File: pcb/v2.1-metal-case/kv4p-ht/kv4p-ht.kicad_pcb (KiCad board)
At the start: 4 copper layers, 80 x 47 mm, 71 parts, among them J1 Antenna, J5 USB-C Socket, Q1 SS8050, Q2 SS8050, Q3 AO3400A, SW3 Reset, SW4 Program, U1 DRA/SA818, U2 AZ1117H-3.3TRG1, U4 CP2102N-A02-GQFN24, U5 ESP32-WROOM-32E-N4

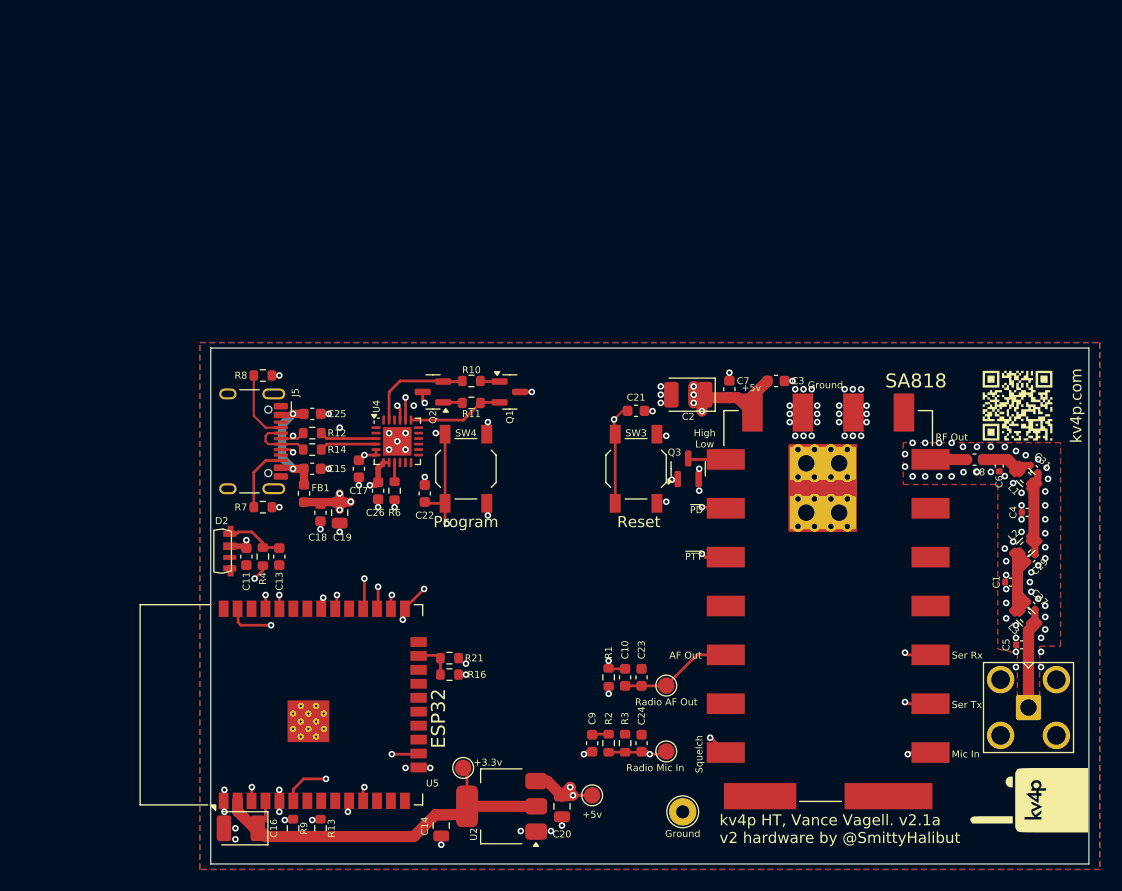
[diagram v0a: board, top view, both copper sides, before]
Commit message: Working on a different case version of kv4p board.
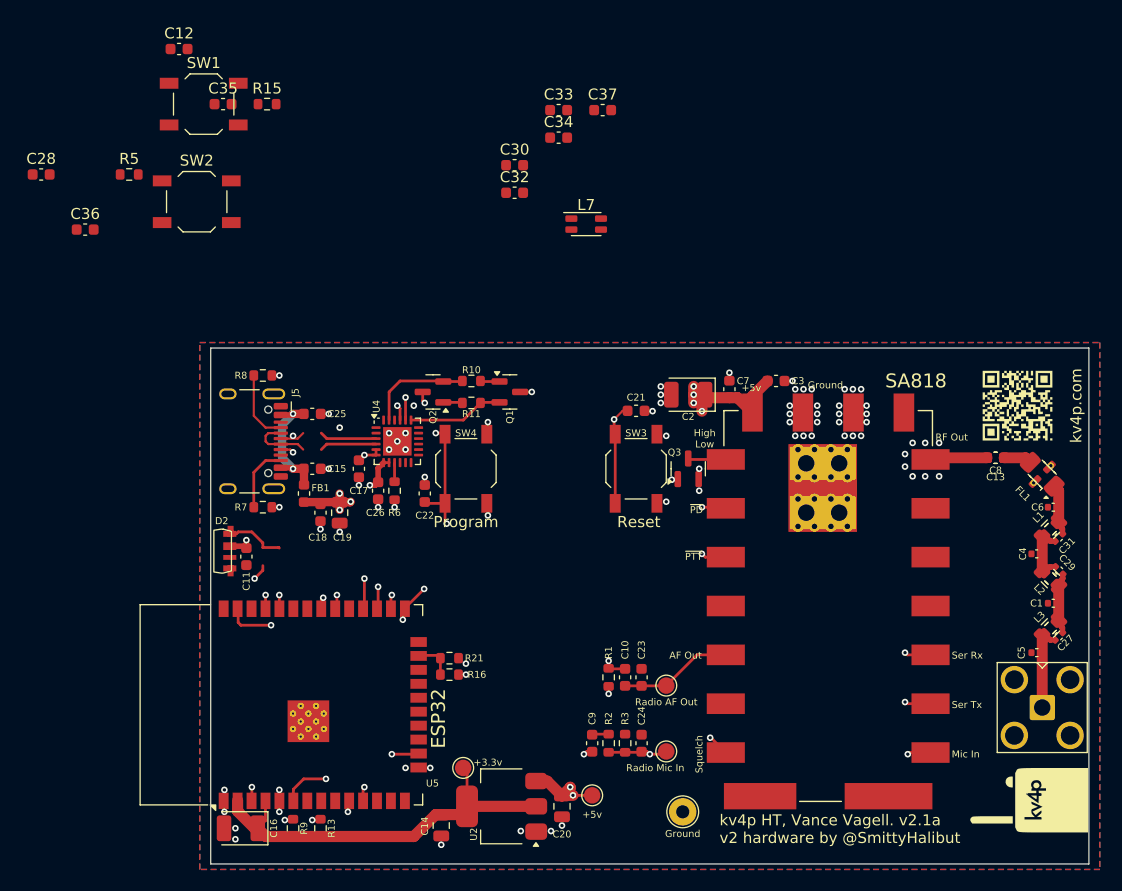
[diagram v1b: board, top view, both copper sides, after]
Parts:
- added C12: 2.2nF Tuned VHF, Capacitor_SMD:C_0603_1608Metric, F.Cu at (187.1, 43.3)
- added C28: 2.2nF Tuned VHF, Capacitor_SMD:C_0603_1608Metric, F.Cu at (174.6, 54.7)
- added C30: 220pF Tune UHF, Capacitor_SMD:C_0603_1608Metric, F.Cu at (217.7, 53.8)
- added C32: 220pF Tune UHF, Capacitor_SMD:C_0603_1608Metric, F.Cu at (217.7, 56.4)
- added C33: 220pF Tune UHF, Capacitor_SMD:C_0603_1608Metric, F.Cu at (221.7, 48.8)
- added C34: 220pF Tune UHF, Capacitor_SMD:C_0603_1608Metric, F.Cu at (221.7, 51.3)
- added C35: 220pF Tune UHF, Capacitor_SMD:C_0603_1608Metric, F.Cu at (191.1, 48.3)
- added C36: 220pF Tune UHF, Capacitor_SMD:C_0603_1608Metric, F.Cu at (178.6, 59.7)
- added C37: 220pF Tune UHF, Capacitor_SMD:C_0603_1608Metric, F.Cu at (225.7, 48.8)
- added FL1: LFCN-490+, Filter:Filter_Mini-Circuits_FV1206, F.Cu at (265.8, 82.0)
- added L7: CMCC, Inductor_SMD:L_CommonMode_Wurth_WE-CNSW-1206, F.Cu at (224.2, 59.2)
- added R15: 10k, Resistor_SMD:R_0603_1608Metric, F.Cu at (195.1, 48.3)
- added R17: 0R, Resistor_SMD:R_0603_1608Metric, F.Cu at (266.5, 87.0)
- added R5: 10k, Resistor_SMD:R_0603_1608Metric, F.Cu at (182.6, 54.7)
- added SW1: Program, Button_Switch_SMD:SW_SPST_TL3342, F.Cu at (189.4, 48.3)
- added SW2: Program, Button_Switch_SMD:SW_SPST_TL3342, F.Cu at (188.7, 57.2)
- C13: value 2.2nF Tuned VHF -> 220pF Tune UHF
- R12, R14: value 27R -> 0R
- R4: value 100R -> 0R; footprint Resistor_SMD:R_0603_1608Metric -> Resistor_SMD:R_1206_3216Metric
- moved R4 71.4 mm to (265.8, 82.0), turned to -45 degrees
- moved R12 69.6 mm to (266.5, 96.0), turned to -135 degrees
- moved R14 68.3 mm to (266.5, 91.5), turned to -45 degrees
- moved C13 65.9 mm to (261.5, 80.5), turned to 180 degrees
- moved C31 6.61 mm to (267.2, 87.8), turned to 45 degrees
- moved C6 6.18 mm to (266.8, 85.0), turned to 0 degrees
- moved L1 5.22 mm to (266.5, 87.0), turned to 45 degrees
- moved L6 5.22 mm to (266.5, 87.0), turned to 45 degrees
- moved C1 4.35 mm to (266.8, 93.8)
- moved C4 3.88 mm to (265.2, 89.2)
- moved C27 3.73 mm to (267.2, 96.8), turned to 45 degrees
- moved L2 3.64 mm to (266.5, 91.5), turned to 135 degrees
- moved L5 3.64 mm to (266.5, 91.5), turned to 135 degrees
- moved C29 2.76 mm to (267.3, 90.8), turned to 135 degrees
- moved L3 2.47 mm to (266.5, 96.0), turned to 45 degrees
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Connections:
- C13 pad 1: Net-(D2-DIN) -> Net-(FL1-OUT)
- C13 pad 2: GND -> Net-(U1-ANT)
- C31 pad 2: Net-(C31-Pad2) -> Net-(FL1-IN)
- C6 pad 2: Net-(C31-Pad2) -> Net-(FL1-IN)
- C8 pad 1: Net-(C31-Pad2) -> Net-(FL1-OUT)
- D2 pad 1: Net-(D2-DIN) -> /NeoPixel DI
- L1 pad 2: Net-(C31-Pad2) -> Net-(FL1-IN)
- L6 pad 2: Net-(C31-Pad2) -> Net-(FL1-IN)
- R12 pad 1: Net-(U4-D+) -> Net-(C1-Pad2)
- R12 pad 2: Net-(J5-D+-PadA6) -> Net-(J1-In)
- R14 pad 1: Net-(U4-D-) -> Net-(C29-Pad2)
- R14 pad 2: Net-(J5-D--PadA7) -> Net-(C1-Pad2)
- R4 pad 1: /NeoPixel DI -> Net-(FL1-OUT)
- R4 pad 2: Net-(D2-DIN) -> Net-(FL1-IN)
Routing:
- net Net-(C31-Pad2): track 5.59 -> 0.00 mm
- net Net-(D2-DIN): track 5.44 -> 0.00 mm
- net /NeoPixel DI: track 31.7 -> 37.2 mm
- net Net-(C1-Pad2): track 10.7 -> 5.33 mm
- net Net-(FL1-IN): track 0.00 -> 4.42 mm
- net Net-(C29-Pad2): track 8.84 -> 5.36 mm
- net Net-(FL1-OUT): track 0.00 -> 2.47 mm
- net Net-(U1-ANT): track 3.31 -> 5.21 mm
- net Net-(J1-In): track 9.06 -> 7.63 mm
- net GND: vias 121 -> 73
